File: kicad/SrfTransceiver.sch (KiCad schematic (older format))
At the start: 52 parts

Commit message: New rx-tx bidirectional amplifier
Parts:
- removed C? (x2): 100n, symbol device:C
- added C?: 68n, symbol device:C
- added R? (x2): 2k2, symbol device:R
- added T?: Transformer_1P_1S, symbol device:Transformer_1P_1S
- Q?: value BC546 -> 2N3904
- R?: value 15k -> 27k
- R?: value 15k -> 22k or 18k
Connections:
- wire segments 156 -> 160
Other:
- note added: "http://qrplw3dyl.blogspot.com/2013/05/amplificador-bilateral-ru3gm.html"
- note added: "http://qrplw3dyl.blogspot.com/2014/02/el-txiki-de-pedro.html"
- moved on the sheet: C?, D?, J?, L?, R?, U?, Y?

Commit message: New rx-tx bidirectional amplifier
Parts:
- removed C? (x6): 100p, symbol device:C
- removed C? (x3): 100n, symbol device:C
- removed C? (x12): 1u, symbol device:C
- removed C? (x2): 10n, symbol device:C
- removed C?: 68n, symbol device:C
- removed D? (x4): 1N4148, symbol device:D
- removed J?: 50 Ohm Antenna, symbol conn:Conn_Coaxial
- removed L? (x7): L, symbol device:L
- removed Q?: 2N3904, TO_SOT_Packages_THT:TO-92_Molded_Narrow, symbol transistors:BC546
- removed Q?: BC546, TO_SOT_Packages_THT:TO-92_Molded_Narrow, symbol transistors:BC546
- removed R?: 27k, symbol device:R
- removed R?: 22k or 18k, symbol device:R
- removed R? (x2): 560, symbol device:R
- removed R? (x2): 2k2, symbol device:R
- removed R? (x2): 15k, symbol device:R
- removed T?: Transformer_1P_1S, symbol device:Transformer_1P_1S
- removed U?: Si4464, Package_DFN_QFN:QFN-20-1EP_4x4mm_P0.5mm_EP2.6x2.6mm_ThermalVias, symbol RF:Si4464
- removed U?: ADE-1+, RF_Mini-Circuits:Mini-Circuits_CD542_LandPatternPL-052, symbol RF_Mixer:ADE-1+
- removed U? (x2): TLV70245_SOT23-5, TO_SOT_Packages_SMD:SOT-23-5, symbol regul:TLV70245_SOT23-5
- removed U?: LM1117-3.3, symbol regul:LM1117-3.3
- removed Y?: 30 MHz, symbol device:Crystal
- removed Y?: Si500D, Si500D, symbol Si500D:Si500D
- added C? (x16): 100p, symbol device:C
- added C?: 100n, symbol device:C
- added C? (x12): 1u, symbol device:C
- added J?: 50 Ohm Antenna, symbol conn:Conn_Coaxial
- added L? (x7): L, symbol device:L
- added U?: Si4464, Package_DFN_QFN:QFN-20-1EP_4x4mm_P0.5mm_EP2.6x2.6mm_ThermalVias, symbol RF:Si4464
- added U?: ADE-1+, RF_Mini-Circuits:Mini-Circuits_CD542_LandPatternPL-052, symbol RF_Mixer:ADE-1+
- added U? (x2): TLV70245_SOT23-5, TO_SOT_Packages_SMD:SOT-23-5, symbol regul:TLV70245_SOT23-5
- added U?: LM1117-3.3, symbol regul:LM1117-3.3
- added U? (x4): MAX2650, smd-semi:SOT-143, symbol maxim_1:MAX2650
- added Y?: 30 MHz, symbol device:Crystal
- added Y?: Si500D, Si500D, symbol Si500D:Si500D
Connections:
- wire segments 160 -> 150
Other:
- note removed: "http://qrplw3dyl.blogspot.com/2013/05/amplificador-bilateral-ru3gm.html"
- note removed: "http://qrplw3dyl.blogspot.com/2014/02/el-txiki-de-pedro.html"

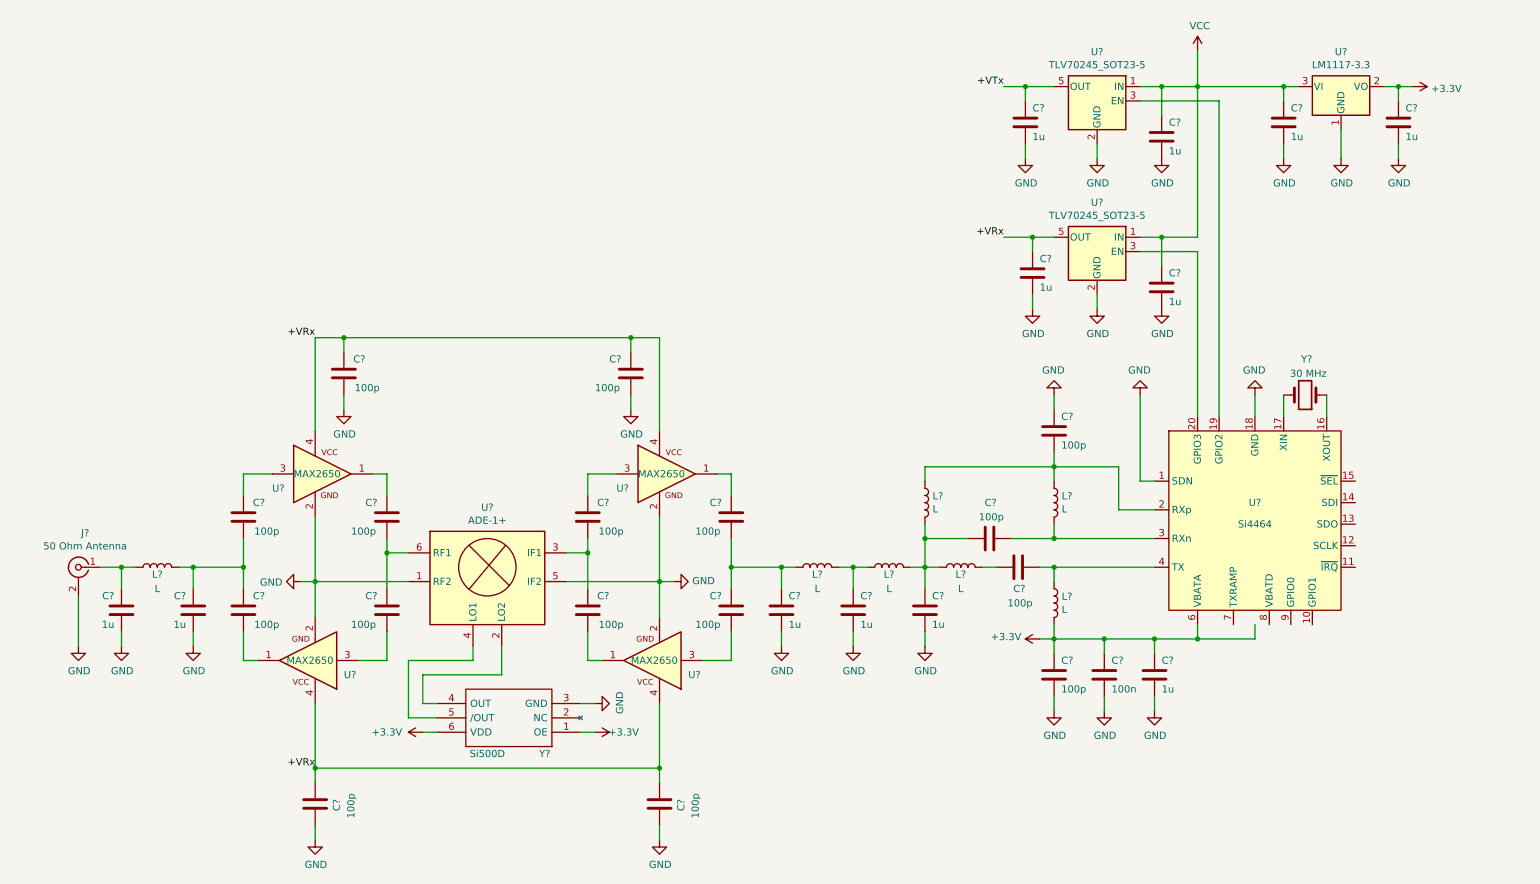
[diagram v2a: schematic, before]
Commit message: New rx-tx bidirectional amplifier
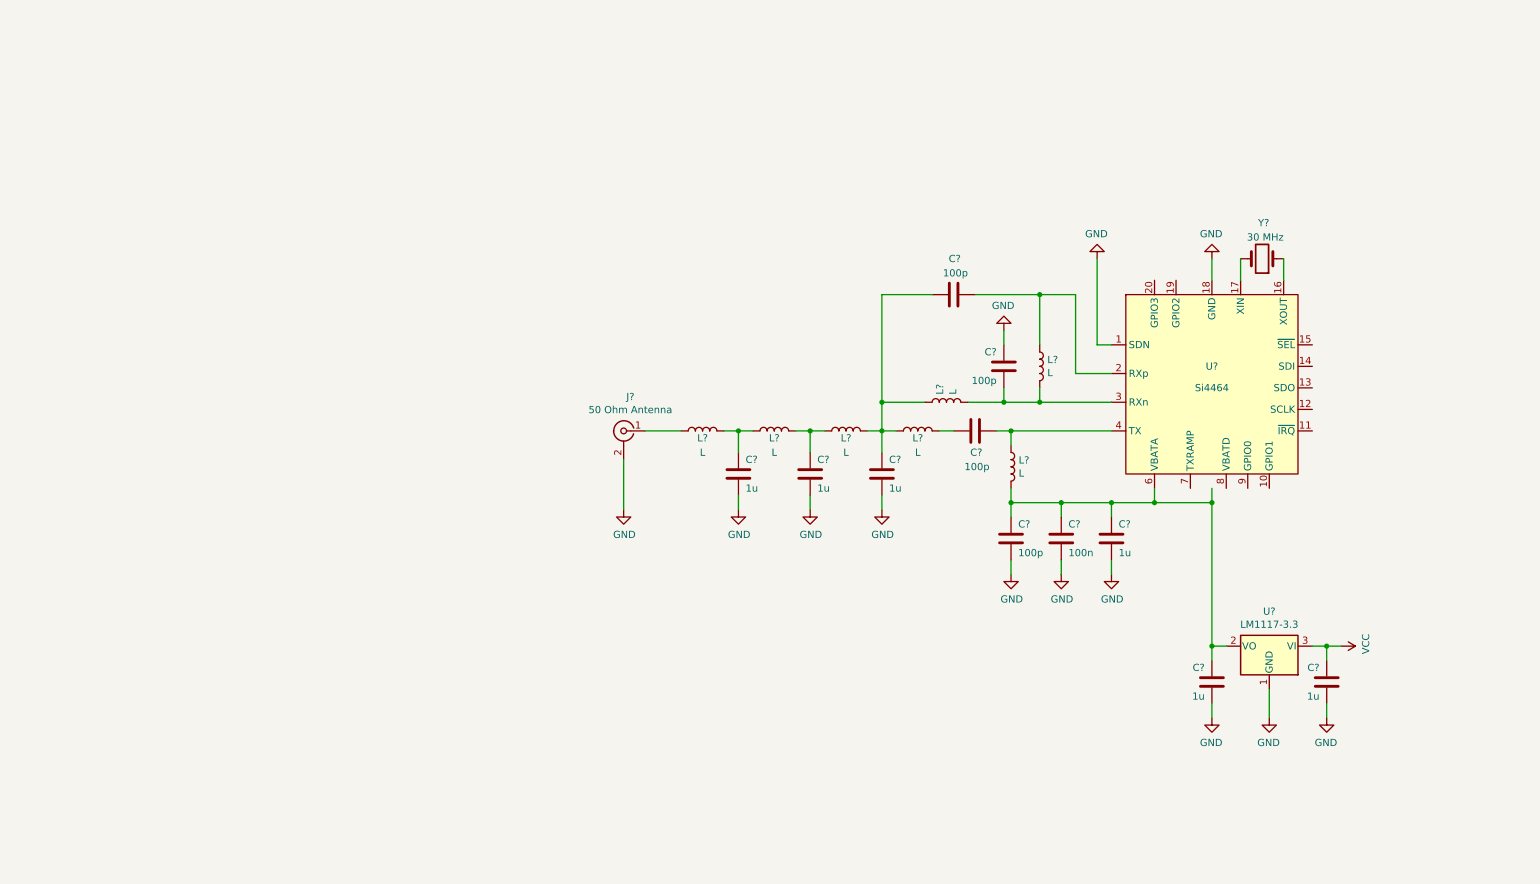
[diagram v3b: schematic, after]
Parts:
- removed C? (x6): 1u, symbol device:C
- removed C? (x12): 100p, symbol device:C
- removed U?: ADE-1+, RF_Mini-Circuits:Mini-Circuits_CD542_LandPatternPL-052, symbol RF_Mixer:ADE-1+
- removed U? (x2): TLV70245_SOT23-5, TO_SOT_Packages_SMD:SOT-23-5, symbol regul:TLV70245_SOT23-5
- removed U? (x4): MAX2650, smd-semi:SOT-143, symbol maxim_1:MAX2650
- removed Y?: Si500D, Si500D, symbol Si500D:Si500D
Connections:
- net at L?.1, U?.2 (RXp): now also C?.2; no longer C?.2, L?.1
- net at L?.2, U?.3 (RXn): now also C?.2, L?.2; no longer C?.2
- net at C?.1, C?.1, L?.1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: now also L?.1; no longer L?.2
- net at L?.2: now also C?.1, L?.1
- net +3V3: no longer names the net of C?.1, C?.1, C?.1, C?.1, L?.2, U?.2 (VO), U?.6 (VBATA)
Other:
- moved on the sheet: C?, J?, L?, U?, Y?

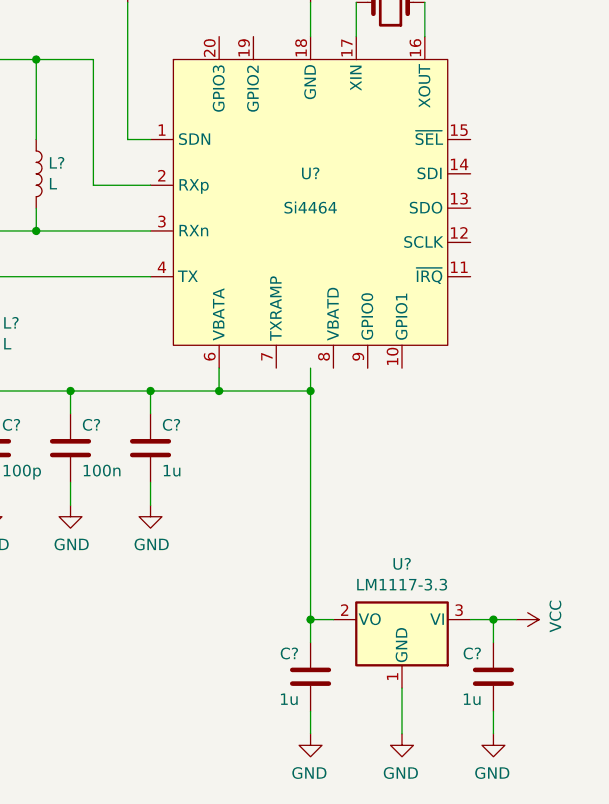
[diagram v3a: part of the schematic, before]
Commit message: Using ERF32FG12 SoC instead of PIC32MX
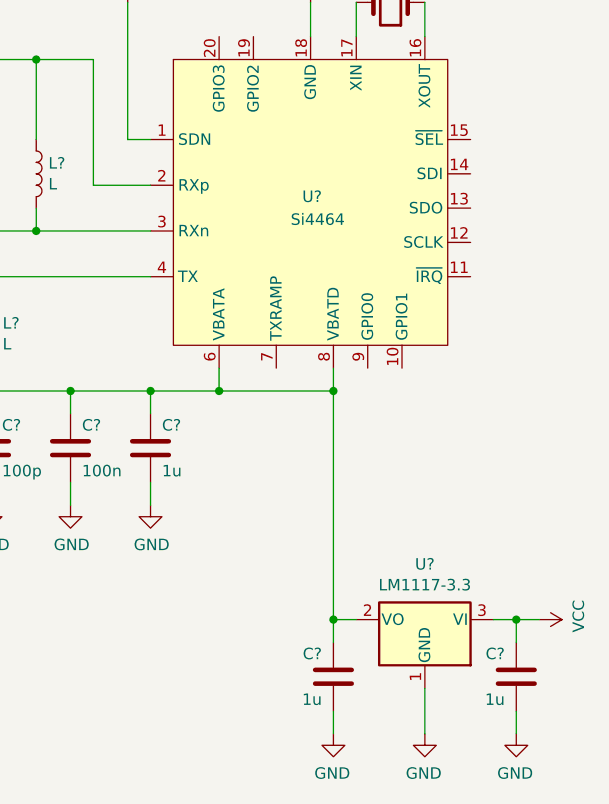
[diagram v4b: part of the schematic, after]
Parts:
- removed U?: Si4464, Package_DFN_QFN:QFN-20-1EP_4x4mm_P0.5mm_EP2.6x2.6mm_ThermalVias, symbol RF:Si4464
- added U?: Si4464, Package_DFN_QFN:QFN-20-1EP_4x4mm_P0.5mm_EP2.6x2.6mm_ThermalVias, symbol RF:Si4464
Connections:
- net GND: now also U?.1 (SDN), U?.18 (GND), U?.21 (GND)
- net at Y?.1: now also U?.16 (XOUT)
- net at Y?.2: now also U?.17 (XIN)
- net at C?.2, L?.1: now also U?.2 (RXp)
- net at C?.2, L?.2, L?.2: now also U?.3 (RXn)
- net at C?.2, L?.1: now also U?.4 (TX)
- net at C?.1, C?.1, C?.1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: now also U?.6 (VBATA), U?.8 (VBATD)
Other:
- moved on the sheet: C?, U?
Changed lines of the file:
@@
 $Descr A4 11693 8268
 encoding utf-8
-Sheet 6 11
+Sheet 6 13
 Title ""
 Date ""
@@
 	7550 4850 7550 4950
 Wire Wire Line
-	8950 4350 8950 4450
-Wire Wire Line
-	8950 4450 8550 4450
+	9050 4350 9050 4450
+Wire Wire Line
+	9050 4450 8550 4450
 Wire Wire Line
 	8550 4450 8550 4350
@@
 L power:VCC #PWR?
 U 1 1 607BEC95
-P 9850 5450
+P 9950 5450
 AR Path="/5038E44C/5FCACBA1/607BEC95" Ref="#PWR?"  Part="1"
 AR Path="/5038E44C/5FCACB2A/607BEC95" Ref="#PWR?"  Part="1"
-F 0 "#PWR?" H 9850 5300 50  0001 C CNN
-F 1 "VCC" H 9865 5623 50  0000 C CNN
-F 2 "" H 9850 5450 50  0001 C CNN
-F 3 "" H 9850 5450 50  0001 C CNN
-	1    9850 5450
+F 0 "#PWR?" H 9950 5300 50  0001 C CNN
+F 1 "VCC" H 9965 5623 50  0000 C CNN
+F 2 "" H 9950 5450 50  0001 C CNN
+F 3 "" H 9950 5450 50  0001 C CNN
+	1    9950 5450
 	0    1    -1   0
 $EndComp
@@
 L regul:LM1117-3.3 U?
 U 1 1 607BECA2
-P 9350 5450
+P 9450 5450
 AR Path="/5038E44C/5FCACBA1/607BECA2" Ref="U?"  Part="1"
 AR Path="/5038E44C/5FCACB2A/607BECA2" Ref="U?"  Part="1"
-F 0 "U?" H 9350 5692 50  0000 C CNN
-F 1 "LM1117-3.3" H 9350 5601 50  0000 C CNN
-F 2 "" H 9350 5450 50  0001 C CNN
-F 3 "http://www.ti.com/lit/ds/symlink/lm1117.pdf" H 9350 5450 50  0001 C CNN
-	1    9350 5450
-	-1   0    0    -1
-$EndComp
-Wire Wire Line
-	9850 5450 9750 5450
+F 0 "U?" H 9450 5692 50  0000 C CNN
+F 1 "LM1117-3.3" H 9450 5601 50  0000 C CNN
+F 2 "" H 9450 5450 50  0001 C CNN
+F 3 "http://www.ti.com/lit/ds/symlink/lm1117.pdf" H 9450 5450 50  0001 C CNN
+	1    9450 5450
+	-1   0    0    -1
+$EndComp
+Wire Wire Line
+	9950 5450 9850 5450
 $Comp
 L power:GND #PWR?
 U 1 1 607BECA9
-P 9350 5950
+P 9450 5950
 AR Path="/5038E44C/5FCACB2A/607BECA9" Ref="#PWR?"  Part="1"
 AR Path="/5038E44C/5FCACBA1/607BECA9" Ref="#PWR?"  Part="1"
-F 0 "#PWR?" H 9350 5700 50  0001 C CNN
-F 1 "GND" H 9355 5777 50  0000 C CNN
-F 2 "" H 9350 5950 50  0001 C CNN
-F 3 "" H 9350 5950 50  0001 C CNN
-	1    9350 5950
-	-1   0    0    -1
-$EndComp
-Wire Wire Line
-	9350 5750 9350 5950
-Wire Wire Line
-	9050 5450 8950 5450
+F 0 "#PWR?" H 9450 5700 50  0001 C CNN
+F 1 "GND" H 9455 5777 50  0000 C CNN
+F 2 "" H 9450 5950 50  0001 C CNN
+F 3 "" H 9450 5950 50  0001 C CNN
+	1    9450 5950
+	-1   0    0    -1
+$EndComp
+Wire Wire Line
+	9450 5750 9450 5950
+Wire Wire Line
+	9150 5450 9050 5450
 $Comp
 L device:C C?
 U 1 1 607BECB7
-P 8950 5700
+P 9050 5700
 AR Path="/5038E44C/5FCACB2A/607BECB7" Ref="C?"  Part="1"
 AR Path="/5038E44C/5FCACBA1/607BECB7" Ref="C?"  Part="1"
-F 0 "C?" H 9000 5800 50  0000 L CNN
-F 1 "1u" H 9000 5600 50  0000 L CNN
-F 2 "" H 8988 5550 50  0001 C CNN
-F 3 "" H 8950 5700 50  0001 C CNN
-	1    8950 5700
+F 0 "C?" H 9100 5800 50  0000 L CNN
+F 1 "1u" H 9100 5600 50  0000 L CNN
+F 2 "" H 9088 5550 50  0001 C CNN
+F 3 "" H 9050 5700 50  0001 C CNN
+	1    9050 5700
 	-1   0    0    -1
 $EndComp
@@
 L power:GND #PWR?
 U 1 1 607BECBD
-P 8950 5950
+P 9050 5950
 AR Path="/5038E44C/5FCACB2A/607BECBD" Ref="#PWR?"  Part="1"
 AR Path="/5038E44C/5FCACBA1/607BECBD" Ref="#PWR?"  Part="1"
-F 0 "#PWR?" H 8950 5700 50  0001 C CNN
-F 1 "GND" H 8955 5777 50  0000 C CNN
-F 2 "" H 8950 5950 50  0001 C CNN
-F 3 "" H 8950 5950 50  0001 C CNN
-	1    8950 5950
-	-1   0    0    -1
-$EndComp
-Wire Wire Line
-	8950 5850 8950 5950
-Wire Wire Line
-	8950 5550 8950 5450
+F 0 "#PWR?" H 9050 5700 50  0001 C CNN
+F 1 "GND" H 9055 5777 50  0000 C CNN
+F 2 "" H 9050 5950 50  0001 C CNN
+F 3 "" H 9050 5950 50  0001 C CNN
+	1    9050 5950
+	-1   0    0    -1
+$EndComp
+Wire Wire Line
+	9050 5850 9050 5950
+Wire Wire Line
+	9050 5550 9050 5450
 $Comp
 L device:C C?
 U 1 1 607BECC7
-P 9750 5700
+P 9850 5700
 AR Path="/5038E44C/5FCACB2A/607BECC7" Ref="C?"  Part="1"
 AR Path="/5038E44C/5FCACBA1/607BECC7" Ref="C?"  Part="1"
-F 0 "C?" H 9800 5800 50  0000 L CNN
-F 1 "1u" H 9800 5600 50  0000 L CNN
-F 2 "" H 9788 5550 50  0001 C CNN
-F 3 "" H 9750 5700 50  0001 C CNN
-	1    9750 5700
+F 0 "C?" H 9900 5800 50  0000 L CNN
+F 1 "1u" H 9900 5600 50  0000 L CNN
+F 2 "" H 9888 5550 50  0001 C CNN
+F 3 "" H 9850 5700 50  0001 C CNN
+	1    9850 5700
 	-1   0    0    -1
 $EndComp
@@
 L power:GND #PWR?
 U 1 1 607BECCD
-P 9750 5950
+P 9850 5950
 AR Path="/5038E44C/5FCACB2A/607BECCD" Ref="#PWR?"  Part="1"
 AR Path="/5038E44C/5FCACBA1/607BECCD" Ref="#PWR?"  Part="1"
-F 0 "#PWR?" H 9750 5700 50  0001 C CNN
-F 1 "GND" H 9755 5777 50  0000 C CNN
-F 2 "" H 9750 5950 50  0001 C CNN
-F 3 "" H 9750 5950 50  0001 C CNN
-	1    9750 5950
-	-1   0    0    -1
-$EndComp
-Wire Wire Line
-	9750 5850 9750 5950
-Wire Wire Line
-	9750 5550 9750 5450
-Connection ~ 9750 5450
-Wire Wire Line
-	9750 5450 9650 5450
+F 0 "#PWR?" H 9850 5700 50  0001 C CNN
+F 1 "GND" H 9855 5777 50  0000 C CNN
+F 2 "" H 9850 5950 50  0001 C CNN
+F 3 "" H 9850 5950 50  0001 C CNN
+	1    9850 5950
+	-1   0    0    -1
+$EndComp
+Wire Wire Line
+	9850 5850 9850 5950
+Wire Wire Line
+	9850 5550 9850 5450
+Connection ~ 9850 5450
+Wire Wire Line
+	9850 5450 9750 5450
 Wire Wire Line
 	4850 4500 4850 4150
@@
 $EndComp
 Wire Wire Line
-	8950 5450 8950 4450
-Connection ~ 8950 5450
-Connection ~ 8950 4450
+	9050 5450 9050 4450
+Connection ~ 9050 5450
 Wire Wire Line
 	7750 3000 7300 3000
@@
 	-1   0    0    1
 $EndComp
-$Comp
-L RF:Si4464 U?
-U 1 1 607BEA24
-P 8950 3650
-F 0 "U?" H 8950 3800 50  0000 C CNN
-F 1 "Si4464" H 8950 3650 50  0000 C CNN
-F 2 "Package_DFN_QFN:QFN-20-1EP_4x4mm_P0.5mm_EP2.6x2.6mm_ThermalVias" H 8950 4850 50  0001 C CNN
-F 3 "https://www.silabs.com/documents/public/data-sheets/Si4464-63-61-60.pdf" H 8650 3550 50  0001 C CNN
-	1    8950 3650
-	1    0    0    -1
-$EndComp
 Wire Wire Line
 	7500 3650 7500 3750
@@
 	6650 3000 6650 3750
 Connection ~ 6650 3750
+$Comp
+L RF:Si4464 U?
+U 1 1 5FEF7E3D
+P 8950 3650
+F 0 "U?" H 9000 3700 50  0000 R CNN
+F 1 "Si4464" H 9100 3600 50  0000 R CNN
+F 2 "Package_DFN_QFN:QFN-20-1EP_4x4mm_P0.5mm_EP2.6x2.6mm_ThermalVias" H 8950 4850 50  0001 C CNN
+F 3 "https://www.silabs.com/documents/public/data-sheets/Si4464-63-61-60.pdf" H 9050 3550 50  0001 C CNN
+	1    8950 3650
+	1    0    0    -1
+$EndComp
+Connection ~ 9050 4450
 $EndSCHEMATC
